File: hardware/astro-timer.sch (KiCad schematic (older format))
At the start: 32 parts, among them J1 AVR-ISP-6, J2 AudioJack3, Q1 Q_NPN_BEC, Q2 Q_NPN_BEC, SW1 SW_SPST, SW2 SW_Push, SW3 SW_Push, SW4 Rotary_Encoder_Switch, U1 ATmega328P-AU, Y1 Crystal

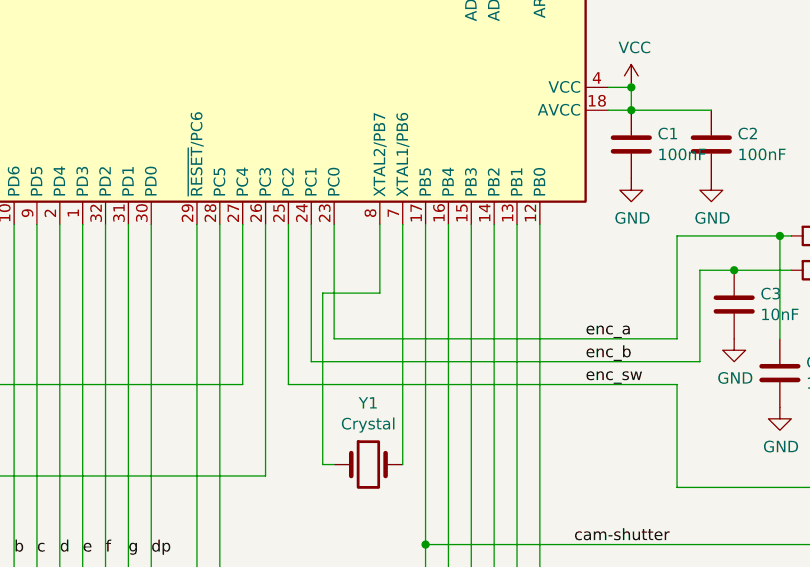
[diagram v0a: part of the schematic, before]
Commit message: make room for the crystal to lie flat on the board
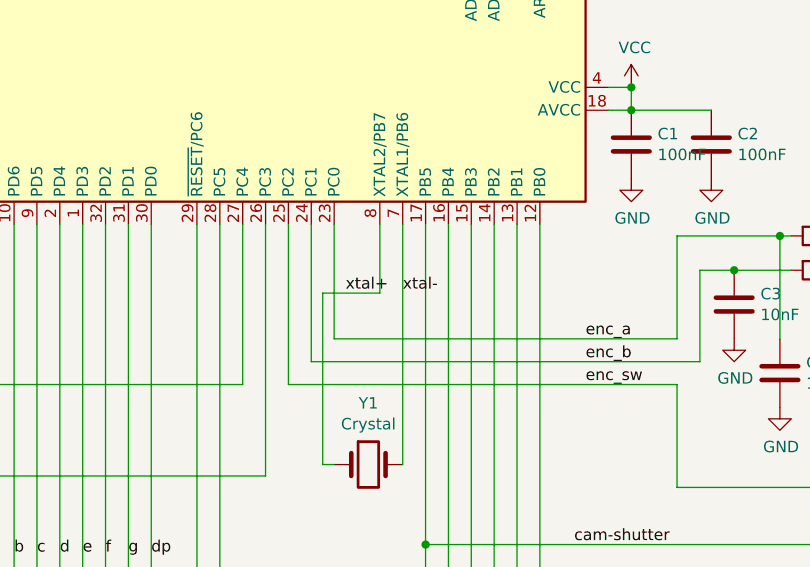
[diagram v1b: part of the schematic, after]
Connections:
- net xtal+: now reaches U1.8 (XTAL2/PB7), Y1.1
- net xtal-: now reaches U1.7 (XTAL1/PB6), Y1.2
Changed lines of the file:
@@
 	1    0    0    -1
 $EndComp
+Text Label 4950 2850 0    50   ~ 0
+xtal+
+Text Label 5200 2850 0    50   ~ 0
+xtal-
 $EndSCHEMATC

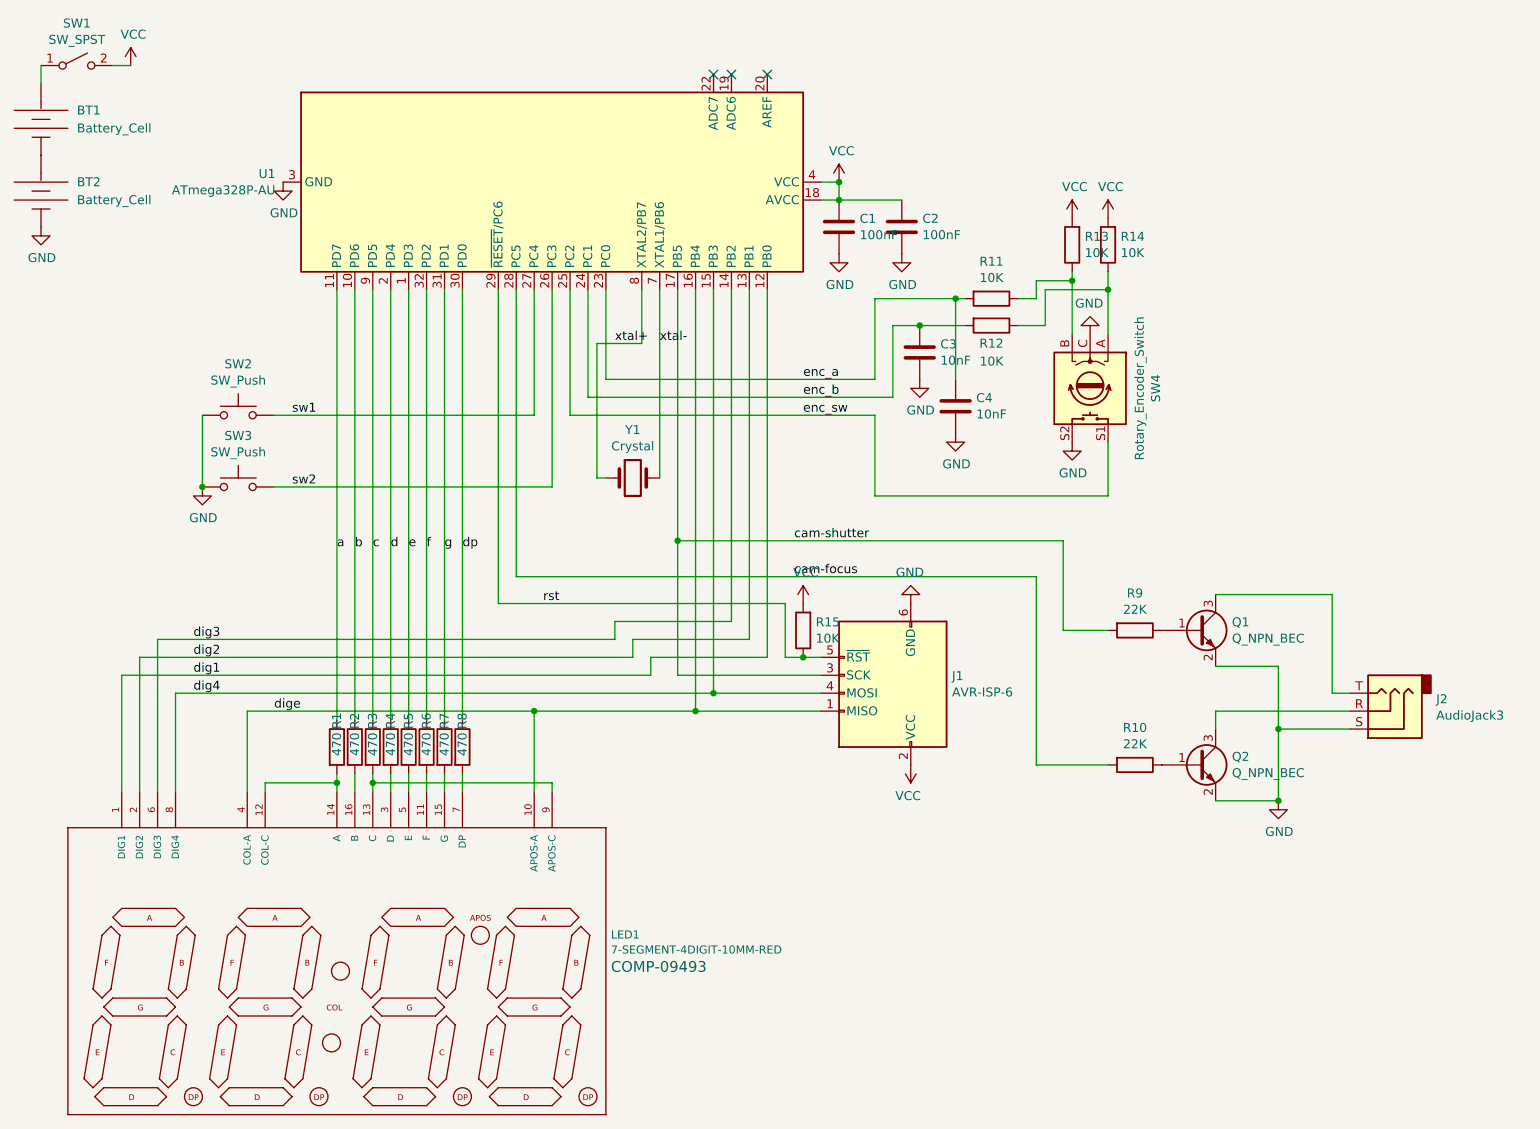
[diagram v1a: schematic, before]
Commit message: lose the hard power switch, lose the screws
make the enclosure snap together!

also get rid of the external pullups on the rotary encoder,
so if it stops between detents, they no longer pull battery
power while the device sleeps
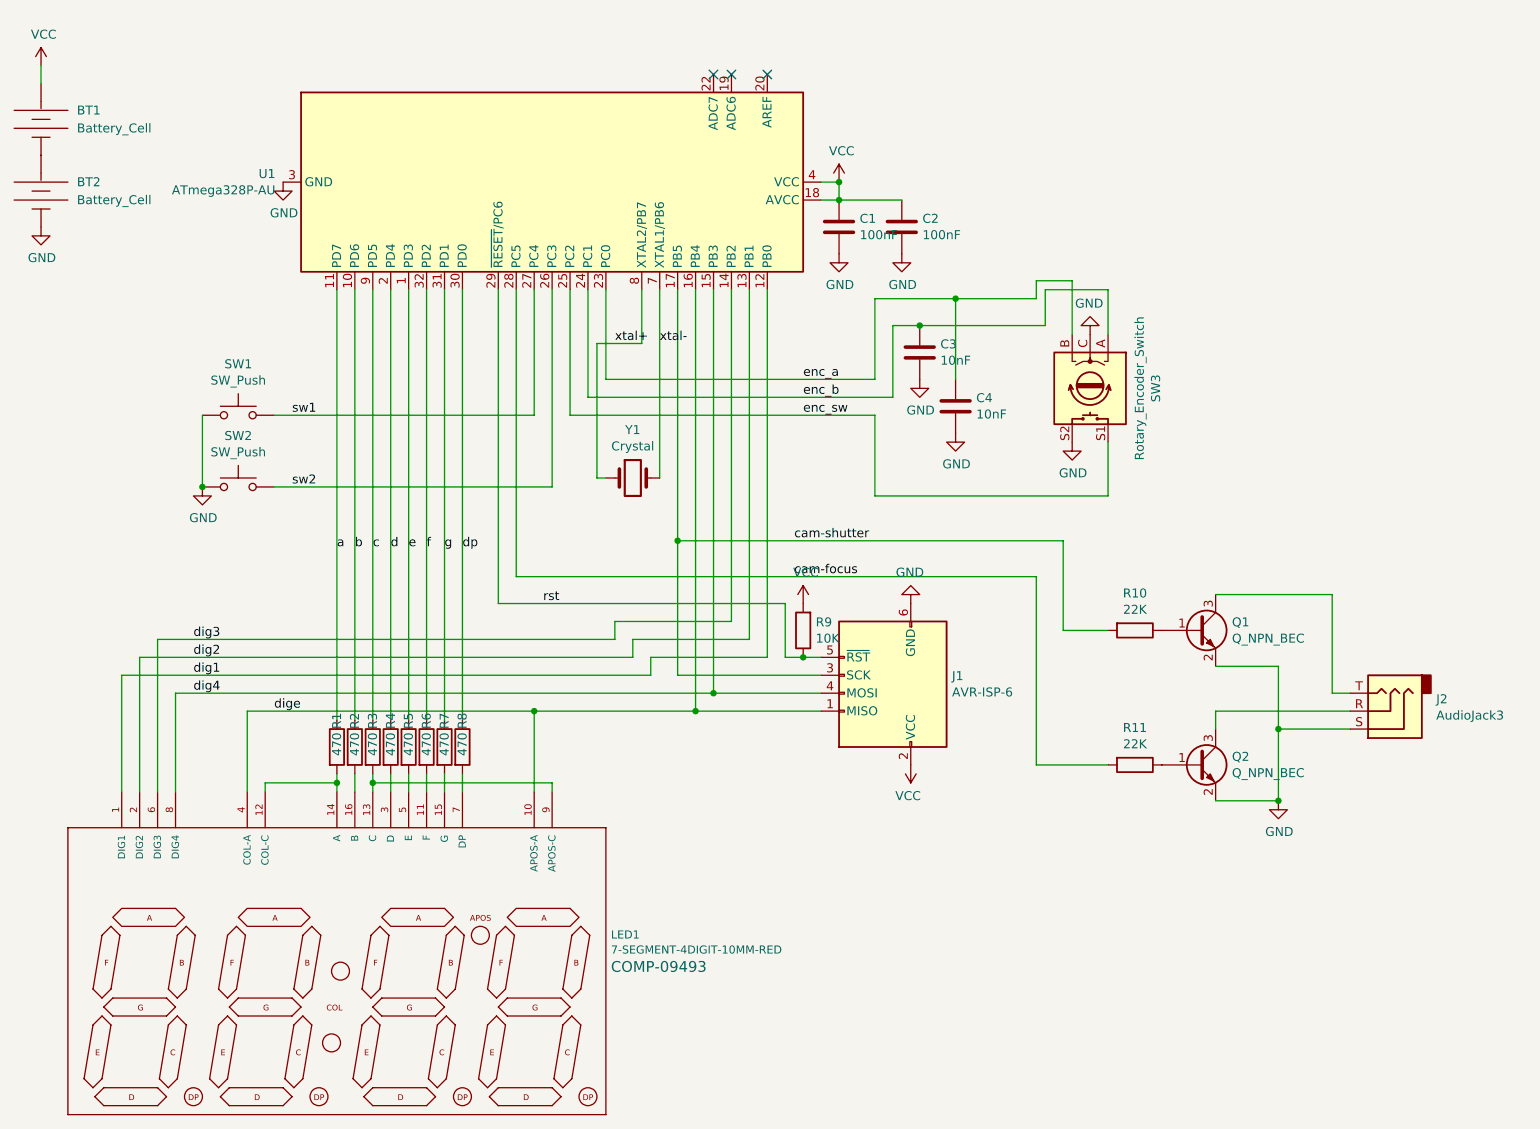
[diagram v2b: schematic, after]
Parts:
- removed R11, R12, R13, R14: 10K, Resistor_SMD:R_0603_1608Metric, symbol Device:R
- removed SW1: SW_SPST, digikey:Switch_Slide_11.6x4mm_EG1218, symbol Switch:SW_SPST
- renumbered R9 to R10, R10 to R11, R15 to R9, SW2 to SW1, SW3 to SW2, SW4 to SW3
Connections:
- net VCC: now also BT1.PWR@ (+)
- net enc_a: now also SW3.B
- net enc_b: now also SW3.A
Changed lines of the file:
@@
 	2500 4800 2500 5350
 $Comp
-L Device:R R9
+L Device:R R10
 U 1 1 60339C31
 P 7850 4450
-F 0 "R9" V 7643 4450 50  0000 C CNN
+F 0 "R10" V 7643 4450 50  0000 C CNN
 F 1 "22K" V 7734 4450 50  0000 C CNN
 F 2 "Resistor_SMD:R_0603_1608Metric" V 7780 4450 50  0001 C CNN
@@
 $EndComp
 $Comp
-L power:GND #PWR012
+L power:GND #PWR015
 U 1 1 6033DA78
 P 8650 5400
-F 0 "#PWR012" H 8650 5150 50  0001 C CNN
+F 0 "#PWR015" H 8650 5150 50  0001 C CNN
 F 1 "GND" H 8655 5227 50  0000 C CNN
 F 2 "" H 8650 5400 50  0001 C CNN
@@
 $EndComp
 $Comp
-L power:VCC #PWR05
+L power:VCC #PWR06
 U 1 1 60347E38
 P 6200 1950
-F 0 "#PWR05" H 6200 1800 50  0001 C CNN
+F 0 "#PWR06" H 6200 1800 50  0001 C CNN
 F 1 "VCC" H 6215 2123 50  0000 C CNN
 F 2 "" H 6200 1950 50  0001 C CNN
@@
 $EndComp
 $Comp
-L power:VCC #PWR09
+L power:VCC #PWR010
 U 1 1 603488D1
 P 6600 5200
-F 0 "#PWR09" H 6600 5050 50  0001 C CNN
+F 0 "#PWR010" H 6600 5050 50  0001 C CNN
 F 1 "VCC" H 6615 5373 50  0000 C CNN
 F 2 "" H 6600 5200 50  0001 C CNN
@@
 $EndComp
 $Comp
-L power:GND #PWR06
+L power:GND #PWR07
 U 1 1 60528475
 P 6200 2350
-F 0 "#PWR06" H 6200 2100 50  0001 C CNN
+F 0 "#PWR07" H 6200 2100 50  0001 C CNN
 F 1 "GND" H 6205 2177 50  0000 C CNN
 F 2 "" H 6200 2350 50  0001 C CNN
@@
 	4300 2550 4300 4300
 $Comp
-L Switch:SW_Push SW3
+L Switch:SW_Push SW2
 U 1 1 60308A52
 P 2850 3650
-F 0 "SW3" H 2850 3935 50  0000 C CNN
+F 0 "SW2" H 2850 3935 50  0000 C CNN
 F 1 "SW_Push" H 2850 3844 50  0000 C CNN
 F 2 "Button_Switch_THT:SW_Tactile_Straight_KSA0Axx1LFTR" H 2850 3850 50  0001 C CNN
@@
 $EndComp
 $Comp
-L Switch:SW_Push SW2
+L Switch:SW_Push SW1
 U 1 1 60308FED
 P 2850 3250
-F 0 "SW2" H 2850 3535 50  0000 C CNN
+F 0 "SW1" H 2850 3535 50  0000 C CNN
 F 1 "SW_Push" H 2850 3444 50  0000 C CNN
 F 2 "Button_Switch_THT:SW_Tactile_Straight_KSA0Axx1LFTR" H 2850 3450 50  0001 C CNN
@@
 Connection ~ 2650 3650
 $Comp
-L power:GND #PWR01
+L power:GND #PWR02
 U 1 1 60349228
 P 1750 2200
-F 0 "#PWR01" H 1750 1950 50  0001 C CNN
+F 0 "#PWR02" H 1750 1950 50  0001 C CNN
 F 1 "GND" H 1755 2027 50  0000 C CNN
 F 2 "" H 1750 2200 50  0001 C CNN
@@
 enc_a
 $Comp
-L power:VCC #PWR02
+L power:VCC #PWR01
 U 1 1 60348A56
-P 2250 1300
-F 0 "#PWR02" H 2250 1150 50  0001 C CNN
-F 1 "VCC" H 2265 1473 50  0000 C CNN
-F 2 "" H 2250 1300 50  0001 C CNN
-F 3 "" H 2250 1300 50  0001 C CNN
-	1    2250 1300
+P 1750 1300
+F 0 "#PWR01" H 1750 1150 50  0001 C CNN
+F 1 "VCC" H 1765 1473 50  0000 C CNN
+F 2 "" H 1750 1300 50  0001 C CNN
+F 3 "" H 1750 1300 50  0001 C CNN
+	1    1750 1300
 	1    0    0    -1
 $EndComp
@@
 	4700 3250 6400 3250
 $Comp
-L power:GND #PWR011
+L power:GND #PWR013
 U 1 1 60408112
 P 7500 3400
-F 0 "#PWR011" H 7500 3150 50  0001 C CNN
+F 0 "#PWR013" H 7500 3150 50  0001 C CNN
 F 1 "GND" H 7505 3227 50  0000 C CNN
 F 2 "" H 7500 3400 50  0001 C CNN
@@
 Text Label 4550 4300 0    50   ~ 0
 rst
-$Comp
-L Switch:SW_SPST SW1
-U 1 1 603E081C
-P 1950 1300
-F 0 "SW1" H 1950 1535 50  0000 C CNN
-F 1 "SW_SPST" H 1950 1444 50  0000 C CNN
-F 2 "digikey:Switch_Slide_11.6x4mm_EG1218" H 1950 1300 50  0001 C CNN
-F 3 "~" H 1950 1300 50  0001 C CNN
-	1    1950 1300
-	1    0    0    -1
-$EndComp
 Wire Wire Line
 	1750 1300 1750 1400
 Wire Wire Line
-	2150 1300 2250 1300
-Wire Wire Line
 	6400 3700 6400 3250
 $Comp
-L Device:Rotary_Encoder_Switch SW4
+L Device:Rotary_Encoder_Switch SW3
 U 1 1 6041992A
 P 7600 3100
-F 0 "SW4" H 7600 3467 50  0000 C CNN
+F 0 "SW3" H 7600 3467 50  0000 C CNN
 F 1 "Rotary_Encoder_Switch" H 7600 3376 50  0000 C CNN
 F 2 "en11:EN11HSM1AF15" H 7450 3260 50  0001 C CNN
@@
 $EndComp
 $Comp
-L Device:R R10
+L Device:R R11
 U 1 1 604C16D1
 P 7850 5200
-F 0 "R10" V 7643 5200 50  0000 C CNN
+F 0 "R11" V 7643 5200 50  0000 C CNN
 F 1 "22K" V 7734 5200 50  0000 C CNN
 F 2 "Resistor_SMD:R_0603_1608Metric" V 7780 5200 50  0001 C CNN
@@
 	7300 5200 7700 5200
 $Comp
-L power:GND #PWR08
+L power:GND #PWR09
 U 1 1 60349F89
 P 6600 4300
-F 0 "#PWR08" H 6600 4050 50  0001 C CNN
+F 0 "#PWR09" H 6600 4050 50  0001 C CNN
 F 1 "GND" H 6605 4127 50  0000 C CNN
 F 2 "" H 6600 4300 50  0001 C CNN
@@
 	6550 2050 6200 2050
 $Comp
-L power:GND #PWR07
+L power:GND #PWR08
 U 1 1 6055A060
 P 6550 2350
-F 0 "#PWR07" H 6550 2100 50  0001 C CNN
+F 0 "#PWR08" H 6550 2100 50  0001 C CNN
 F 1 "GND" H 6555 2177 50  0000 C CNN
 F 2 "" H 6550 2350 50  0001 C CNN
@@
 	1    0    0    -1
 $EndComp
-$Comp
-L Device:R R11
-U 1 1 604FB125
-P 7050 2600
-F 0 "R11" V 6843 2600 50  0000 C CNN
-F 1 "10K" V 6934 2600 50  0000 C CNN
-F 2 "Resistor_SMD:R_0603_1608Metric" V 6980 2600 50  0001 C CNN
-F 3 "~" H 7050 2600 50  0001 C CNN
-F 4 "C25804" V 7050 2600 50  0001 C CNN "JLC"
-	1    7050 2600
-	0    1    1    0
-$EndComp
-$Comp
-L Device:R R12
-U 1 1 604FB58C
-P 7050 2750
-F 0 "R12" V 7150 2750 50  0000 C CNN
-F 1 "10K" V 7250 2750 50  0000 C CNN
-F 2 "Resistor_SMD:R_0603_1608Metric" V 6980 2750 50  0001 C CNN
-F 3 "~" H 7050 2750 50  0001 C CNN
-F 4 "C25804" V 7050 2750 50  0001 C CNN "JLC"
-	1    7050 2750
-	0    1    1    0
-$EndComp
-$Comp
-L Device:R R13
-U 1 1 604FB812
-P 7500 2300
-F 0 "R13" H 7430 2254 50  0000 R CNN
-F 1 "10K" H 7430 2345 50  0000 R CNN
-F 2 "Resistor_SMD:R_0603_1608Metric" V 7430 2300 50  0001 C CNN
-F 3 "~" H 7500 2300 50  0001 C CNN
-F 4 "C25804" H 7500 2300 50  0001 C CNN "JLC"
-	1    7500 2300
-	-1   0    0    1
-$EndComp
-Wire Wire Line
-	6900 2750 6650 2750
-Wire Wire Line
-	6900 2600 6850 2600
-$Comp
-L Device:R R14
-U 1 1 604FC49A
-P 7700 2300
-F 0 "R14" H 7630 2254 50  0000 R CNN
-F 1 "10K" H 7630 2345 50  0000 R CNN
-F 2 "Resistor_SMD:R_0603_1608Metric" V 7630 2300 50  0001 C CNN
-F 3 "~" H 7700 2300 50  0001 C CNN
-F 4 "C25804" H 7700 2300 50  0001 C CNN "JLC"
-	1    7700 2300
-	-1   0    0    1
-$EndComp
-$Comp
-L power:VCC #PWR016
-U 1 1 60521C1F
-P 7700 2150
-F 0 "#PWR016" H 7700 2000 50  0001 C CNN
-F 1 "VCC" H 7715 2323 50  0000 C CNN
-F 2 "" H 7700 2150 50  0001 C CNN
-F 3 "" H 7700 2150 50  0001 C CNN
-	1    7700 2150
-	1    0    0    -1
-$EndComp
-$Comp
-L power:VCC #PWR014
-U 1 1 6052214C
-P 7500 2150
-F 0 "#PWR014" H 7500 2000 50  0001 C CNN
-F 1 "VCC" H 7515 2323 50  0000 C CNN
-F 2 "" H 7500 2150 50  0001 C CNN
-F 3 "" H 7500 2150 50  0001 C CNN
-	1    7500 2150
-	1    0    0    -1
-$EndComp
 Wire Wire Line
 	7700 3700 7700 3400
 Wire Wire Line
 	6400 3700 7700 3700
-Wire Wire Line
-	7700 2450 7700 2550
-Wire Wire Line
-	7500 2450 7500 2500
-$Comp
-L power:GND #PWR015
+$Comp
+L power:GND #PWR014
 U 1 1 6055082A
 P 7600 2800
-F 0 "#PWR015" H 7600 2550 50  0001 C CNN
+F 0 "#PWR014" H 7600 2550 50  0001 C CNN
 F 1 "GND" H 7605 2627 50  0000 C CNN
 F 2 "" H 7600 2800 50  0001 C CNN
@@
 $EndComp
 Wire Wire Line
-	7200 2600 7300 2600
-Wire Wire Line
 	7300 2600 7300 2500
 Wire Wire Line
 	7300 2500 7500 2500
-Connection ~ 7500 2500
 Wire Wire Line
 	7500 2500 7500 2800
 Wire Wire Line
-	7200 2750 7350 2750
-Wire Wire Line
-	7350 2750 7350 2550
-Wire Wire Line
 	7350 2550 7700 2550
-Connection ~ 7700 2550
 Wire Wire Line
 	7700 2550 7700 2800
@@
 	6850 2600 6400 2600
 $Comp
-L power:GND #PWR013
+L power:GND #PWR012
 U 1 1 6056D312
 P 6850 3350
-F 0 "#PWR013" H 6850 3100 50  0001 C CNN
+F 0 "#PWR012" H 6850 3100 50  0001 C CNN
 F 1 "GND" H 6855 3177 50  0000 C CNN
 F 2 "" H 6850 3350 50  0001 C CNN
@@
 $EndComp
 $Comp
-L power:GND #PWR010
+L power:GND #PWR011
 U 1 1 6056D73C
 P 6650 3050
-F 0 "#PWR010" H 6650 2800 50  0001 C CNN
+F 0 "#PWR011" H 6650 2800 50  0001 C CNN
 F 1 "GND" H 6655 2877 50  0000 C CNN
 F 2 "" H 6650 3050 50  0001 C CNN
@@
 $EndComp
 $Comp
-L Device:R R15
+L Device:R R9
 U 1 1 604FD70B
 P 6000 4450
-F 0 "R15" H 5930 4404 50  0000 R CNN
+F 0 "R9" H 5930 4404 50  0000 R CNN
 F 1 "10K" H 5930 4495 50  0000 R CNN
 F 2 "Resistor_SMD:R_0603_1608Metric" V 5930 4450 50  0001 C CNN
@@
 	6000 4600 5900 4600
 $Comp
-L power:VCC #PWR017
+L power:VCC #PWR05
 U 1 1 604FE3F2
 P 6000 4300
-F 0 "#PWR017" H 6000 4150 50  0001 C CNN
+F 0 "#PWR05" H 6000 4150 50  0001 C CNN
 F 1 "VCC" H 6015 4473 50  0000 C CNN
 F 2 "" H 6000 4300 50  0001 C CNN
@@
 Text Label 5200 2850 0    50   ~ 0
 xtal-
+Wire Wire Line
+	7350 2750 7350 2550
+Wire Wire Line
+	6850 2600 7300 2600
+Wire Wire Line
+	6650 2750 7350 2750
 $EndSCHEMATC
